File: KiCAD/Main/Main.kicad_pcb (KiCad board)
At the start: 4 copper layers, 61.8 x 150 mm, 98 parts, among them J1 Micro_SD_Card_Det2, J2 Screw_Terminal_01x09, J3 Screw_Terminal_01x09, J4 USB_C_Receptacle_USB2.0_16P, J7 Conn_02x05_Top_Bottom_Mountin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, J8 Conn_Coaxial, J9 Conn_Coaxial, Q1 AO3400A, Q2 AO3400A, Q3 AO3400A, Q4 2N7002, SW1 RESET, SW2 USER, U1 LM2596S-3.3, U11 BMP390L, U12 BMP390L, U13 BMP390L, U14 BMI270, U15 BMI270, U16 BMI270, U17 SHT4x, U2 TPS2121RUXR, U3 BMM350, U4 STM32H750VBTx, U5 MAX-M8Q, U7 ISM6HG256x, Y2 SiT8008xx-2x-xxE (25MHz)

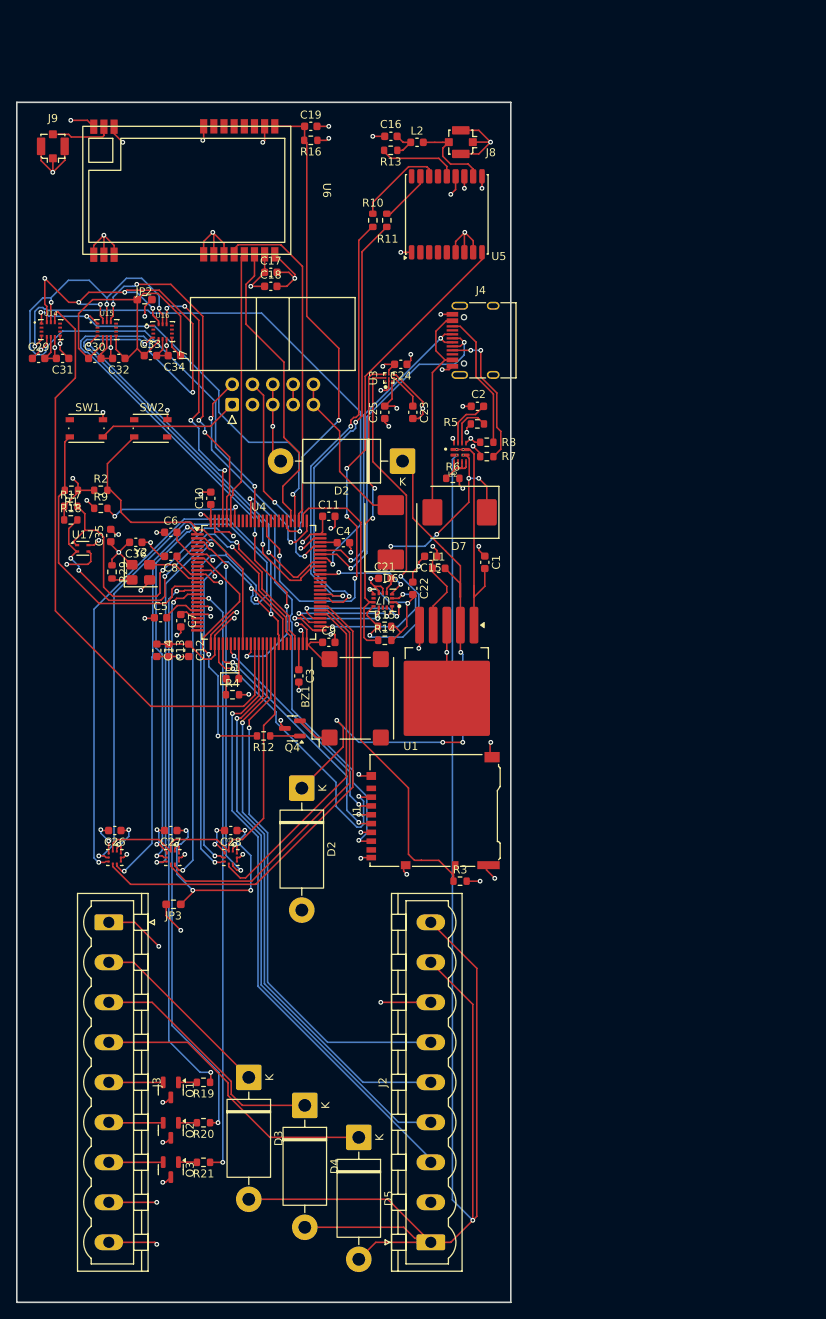
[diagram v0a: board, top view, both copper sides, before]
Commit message: Initial component placement
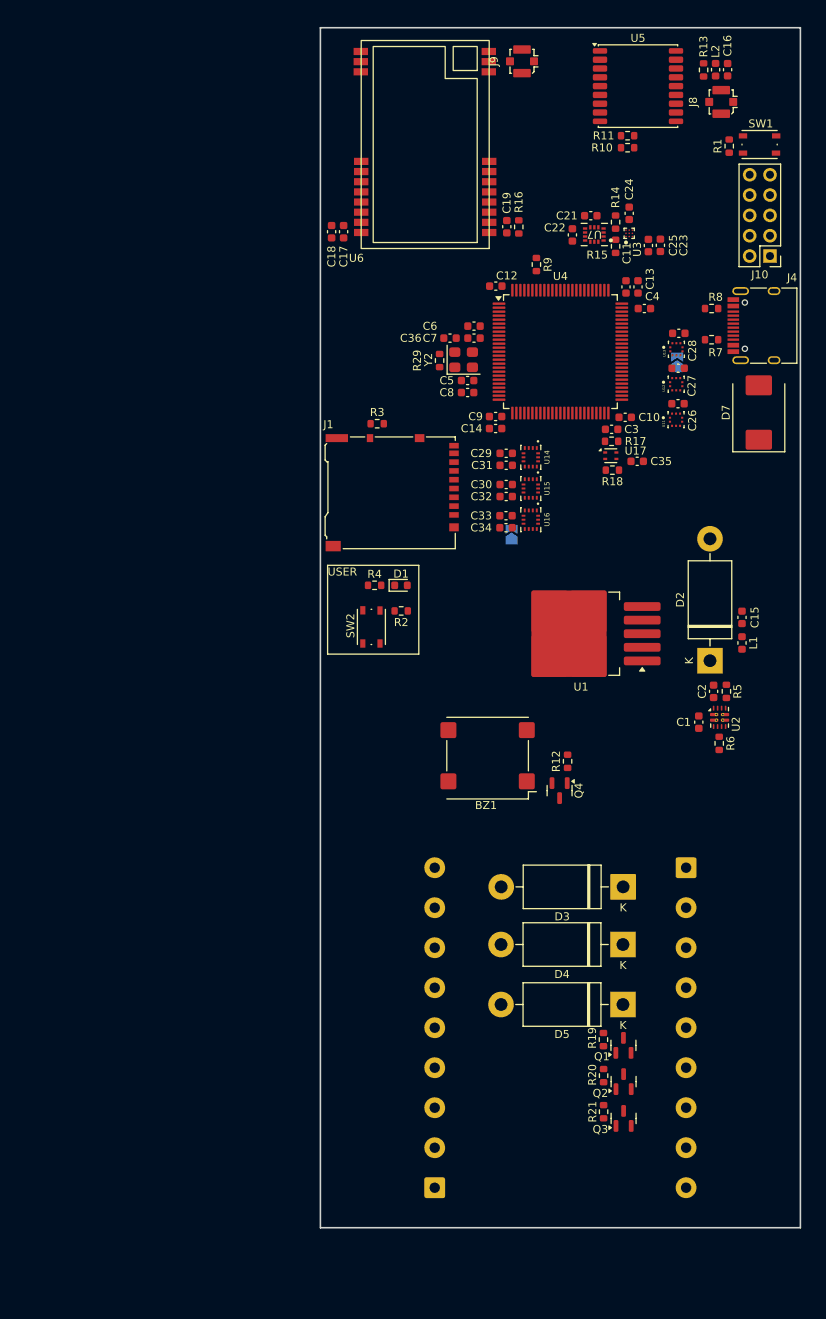
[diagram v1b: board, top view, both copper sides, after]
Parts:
- removed the D2 at (118.0, 84.8)
- removed the D2 at (105.4, 125.7)
- removed D6: MBRS340, Diode_SMD:D_SMC
- removed J7: Conn_02x05_Top_Bottom_MountingPin, Connector_IDC:IDC-Header_2x05_P2.54mm_Horizontal
- added D2: 1N5820, Diode_THT:D_DO-201AD_P15.24mm_Horizontal, F.Cu at (156.4, 109.8)
- added J10: Conn_02x05_Counter_Clockwise, Connector_PinHeader_2.54mm:PinHeader_2x05_P2.54mm_Vertical, F.Cu at (163.9, 59.2)
- J2, J3: footprint Connector_Phoenix_MSTB:PhoenixContact_MSTBVA_2,5_9-G_1x09_P5.00mm_Vertical -> TerminalBlock_Phoenix:TerminalBlock_Phoenix_MKDS-1,5-9_1x09_P5.00mm_Horizontal; moved to B.Cu
- JP2, JP3: footprint Resistor_SMD:R_0603_1608Metric_Pad0.98x0.95mm_HandSolder -> Jumper:SolderJumper-2_P1.3mm_Open_TrianglePad1.0x1.5mm; moved to B.Cu
- U11, U12, U13: footprint BMP390L:XDCR_BMP390L -> LRI:XDCR_BMP390L
- U14, U15, U16: footprint BMI270:XDCR_BMI270 -> LRI:XDCR_BMI270
- U2: footprint TPS2121RUXR:IC_TPS2121RUXR -> Package_DFN_QFN:Texas_VQFN-HR-12_2x2.5mm_P0.5mm_ThermalVias
- U3: footprint BMM350:BGA9C40P3X3_128X128X50 -> LRI:BGA9C40P3X3_128X128X50
- U6: footprint E22-900T22S:E22-900T22S -> LRI:E22-900T22S
- U7: footprint ISM6HG256XTR:U_LGA-14L_2p5X3p0X0p83_STM -> LRI:ISM6
- moved R1 92.8 mm to (158.8, 45.5), turned to 90 degrees
- moved JP3 92.5 mm to (152.3, 72.5), turned to 90 degrees
- moved SW1 91.3 mm to (162.6, 45.3)
- moved U11 89.0 mm to (152.2, 79.7), turned to 90 degrees
- moved C26 88.3 mm to (152.4, 77.7), turned to 0 degrees
- moved U12 86.4 mm to (152.2, 75.2), turned to 90 degrees
- moved C27 85.8 mm to (152.4, 73.2), turned to 0 degrees
- moved U13 84.5 mm to (152.2, 70.9), turned to 90 degrees
- moved C28 83.7 mm to (152.5, 68.9), turned to 0 degrees
- moved C13 74.2 mm to (147.4, 63.1), turned to 90 degrees
- moved J3 72.5 mm to (153.4, 135.7)
- moved R17 68.1 mm to (144.1, 82.4), turned to 180 degrees
- moved R18 68.0 mm to (144.2, 86.0), turned to 180 degrees
- moved U17 67.0 mm to (144.0, 84.2)
- moved C35 66.5 mm to (147.3, 84.9), turned to 0 degrees
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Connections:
- R12 pad 2: Net-(U4-PC13) -> /Microcontroller/BUZZER
- U4 pad 1: /Barometer/BMP390 INT1 -> unconnected-(U4-PE2-Pad1)
- U4 pad 15: /Microcontroller/Drogue Eject Main -> unconnected-(U4-PC0-Pad15)
- U4 pad 16: /Microcontroller/Drogue Eject Backup -> unconnected-(U4-PC1-Pad16)
- U4 pad 17: /Microcontroller/Main Eject -> /Microcontroller/Servo1_Encoder
- U4 pad 18: unconnected-(U4-PC3_C-Pad18) -> /Microcontroller/Servo2_Encoder
- U4 pad 2: /Barometer/BMP390 INT2 -> unconnected-(U4-PE3-Pad2)
- U4 pad 25: unconnected-(U4-PA3-Pad25) -> /Microcontroller/SD_Det
- U4 pad 3: /Barometer/BMP390 INT3 -> /Microcontroller/Drogue Eject Main
- U4 pad 30: unconnected-(U4-PA6-Pad30) -> /Microcontroller/SD_MISO
- U4 pad 33: /Microcontroller/USER_LED -> unconnected-(U4-PC5-Pad33)
- U4 pad 34: /Microcontroller/USER_BTN -> unconnected-(U4-PB0-Pad34)
- U4 pad 35: /Microcontroller/SIMU CS3 -> unconnected-(U4-PB1-Pad35)
- U4 pad 36: /Microcontroller/SIMU MOSI -> /Microcontroller/SIMU1 INT
- U4 pad 38: /Microcontroller/Servo1_DOut -> /Microcontroller/SIMU2 INT
- U4 pad 39: /Microcontroller/Servo2_DOut -> /Microcontroller/SIMU CS2
- U4 pad 4: unconnected-(U4-PE5-Pad4) -> /Microcontroller/Drogue Eject Backup
- U4 pad 40: /Microcontroller/Servo1_Encoder -> /Microcontroller/SIMU3 INT
- U4 pad 41: /Microcontroller/Servo2_Encoder -> /Microcontroller/SIMU CS3
- U4 pad 42: /Barometer/BMP390_SCK -> /Microcontroller/SIMU CLK
- U4 pad 43: /Barometer/BMP390_MISO -> /Microcontroller/SIMU MISO
- U4 pad 44: /Barometer/BMP390_MOSI -> /Microcontroller/SIMU MOSI
- U4 pad 5: unconnected-(U4-PE6-Pad5) -> /Microcontroller/Main Eject
- U4 pad 51: /IMUs/BNO_CS -> unconnected-(U4-PB12-Pad51)
- U4 pad 52: /IMUs/BNO_SCK -> /Barometer/BMP390_SCK
- U4 pad 53: /IMUs/BNO_MISO -> /Barometer/BMP390_MISO
- U4 pad 54: /IMUs/BNO_MOSI -> /Barometer/BMP390_MOSI
- U4 pad 55: /Barometer/BMP390_CS3 -> /Barometer/BMP390_CS1
- U4 pad 56: /Barometer/BMP390_CS2 -> /Barometer/BMP390 INT1
- U4 pad 57: /Barometer/BMP390_CS1 -> /Barometer/BMP390_CS2
- U4 pad 58: unconnected-(U4-PD11-Pad58) -> /Barometer/BMP390 INT2
- U4 pad 59: /GPS/GPS_SCL -> /Barometer/BMP390_CS3
- U4 pad 60: /GPS/GPS_SDA -> /Barometer/BMP390 INT3
- U4 pad 63: unconnected-(U4-PC6-Pad63) -> /Microcontroller/Servo1_DOut
- U4 pad 64: unconnected-(U4-PC7-Pad64) -> /Microcontroller/Servo2_DOut
- U4 pad 65: /IMUs/BNO_INT -> /Microcontroller/BUZZER
- U4 pad 66: unconnected-(U4-PC9-Pad66) -> /Microcontroller/USER_LED
- U4 pad 67: /Microcontroller/SIMU3 INT -> /Microcontroller/USER_BTN
- U4 pad 68: /Microcontroller/SIMU2 INT -> unconnected-(U4-PA9-Pad68)
- U4 pad 69: /Microcontroller/SIMU1 INT -> unconnected-(U4-PA10-Pad69)
- U4 pad 7: Net-(U4-PC13) -> unconnected-(U4-PC13-Pad7)
- U4 pad 77: /Microcontroller/SD_Det -> /IMUs/ISM_INT
- U4 pad 78: /Microcontroller/Radio TX -> /IMUs/ISM_SCK
- U4 pad 79: /Microcontroller/SIMU MISO -> /IMUs/ISM_MISO
- U4 pad 80: /Microcontroller/Radio AUX -> /IMUs/ISM_MOSI
- U4 pad 81: /Microcontroller/Radio RST -> /IMUs/ISM_CS
- U4 pad 86: /GPS/GPS_RESET -> unconnected-(U4-PD5-Pad86)
- U4 pad 89: /Microcontroller/SIMU CLK -> unconnected-(U4-PB3-Pad89)
- U4 pad 90: /Microcontroller/SD_MISO -> unconnected-(U4-PB4-Pad90)
- U4 pad 91: unconnected-(U4-PB5-Pad91) -> /GPS/GPS_RESET
- U4 pad 92: unconnected-(U4-PB6-Pad92) -> /GPS/GPS_SCL
- U4 pad 93: unconnected-(U4-PB7-Pad93) -> /GPS/GPS_SDA
- U4 pad 95: /Microcontroller/Radio RX -> /Microcontroller/Radio RST
- U4 pad 96: unconnected-(U4-PB9-Pad96) -> /Microcontroller/Radio AUX
- U4 pad 97: /Microcontroller/SIMU CS2 -> /Microcontroller/Radio RX
- U4 pad 98: unconnected-(U4-PE1-Pad98) -> /Microcontroller/Radio TX
- U7 pad 1: /IMUs/BNO_MISO -> /IMUs/ISM_MISO
- U7 pad 10: Net-(U3-SCK) -> unconnected-(U7-OCS_Aux-Pad10)
- U7 pad 11: Net-(U3-SDA) -> unconnected-(U7-SDO_Aux-Pad11)
- U7 pad 12: /IMUs/BNO_CS -> /IMUs/ISM_CS
- U7 pad 13: unconnected-(U7-SCL-Pad13) -> /IMUs/ISM_SCK
- U7 pad 14: unconnected-(U7-SDA-Pad14) -> /IMUs/ISM_MOSI
- U7 pad 2: /IMUs/BNO_MOSI -> Net-(U3-SDA)
- U7 pad 3: /IMUs/BNO_SCK -> Net-(U3-SCK)
- U7 pad 4: /IMUs/BNO_INT -> /IMUs/ISM_INT
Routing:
- net GND: track 238.3 -> 0.00 mm, vias 80 -> 0
- net Net-(D3-A): track 229.0 -> 0.00 mm, vias 1 -> 0
- net /Barometer/BMP390_MISO: track 172.7 -> 0.00 mm, vias 5 -> 0
- net /Barometer/BMP390_MOSI: track 167.2 -> 0.00 mm, vias 4 -> 0
- net +3V3: track 157.9 -> 0.00 mm, vias 28 -> 0
- net /Microcontroller/SIMU MOSI: track 121.9 -> 0.00 mm, vias 9 -> 0
- net /Microcontroller/SIMU CLK: track 80.7 -> 0.00 mm, vias 4 -> 0
- net /Microcontroller/SIMU CS1: track 77.7 -> 0.00 mm
- net /Microcontroller/Servo1_DOut: track 77.1 -> 0.00 mm, vias 1 -> 0
- net /Microcontroller/SIMU1 INT: track 74.7 -> 0.00 mm, vias 2 -> 0
- net /Microcontroller/Main Eject: track 74.2 -> 0.00 mm, vias 2 -> 0
- net /Microcontroller/Servo2_DOut: track 73.8 -> 0.00 mm, vias 1 -> 0
- net /Microcontroller/Drogue Eject Backup: track 72.2 -> 0.00 mm, vias 2 -> 0
- net /Microcontroller/Servo1_Encoder: track 71.0 -> 0.00 mm, vias 1 -> 0
- net Net-(D2-K): track 70.5 -> 0.00 mm, vias 4 -> 0
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- removed copper zone on In2.Cu, net +3V3
- removed copper zone on In1.Cu, net GND
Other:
- board size 61.8 x 150 mm -> 60 x 150 mm
- board text added: "USER"

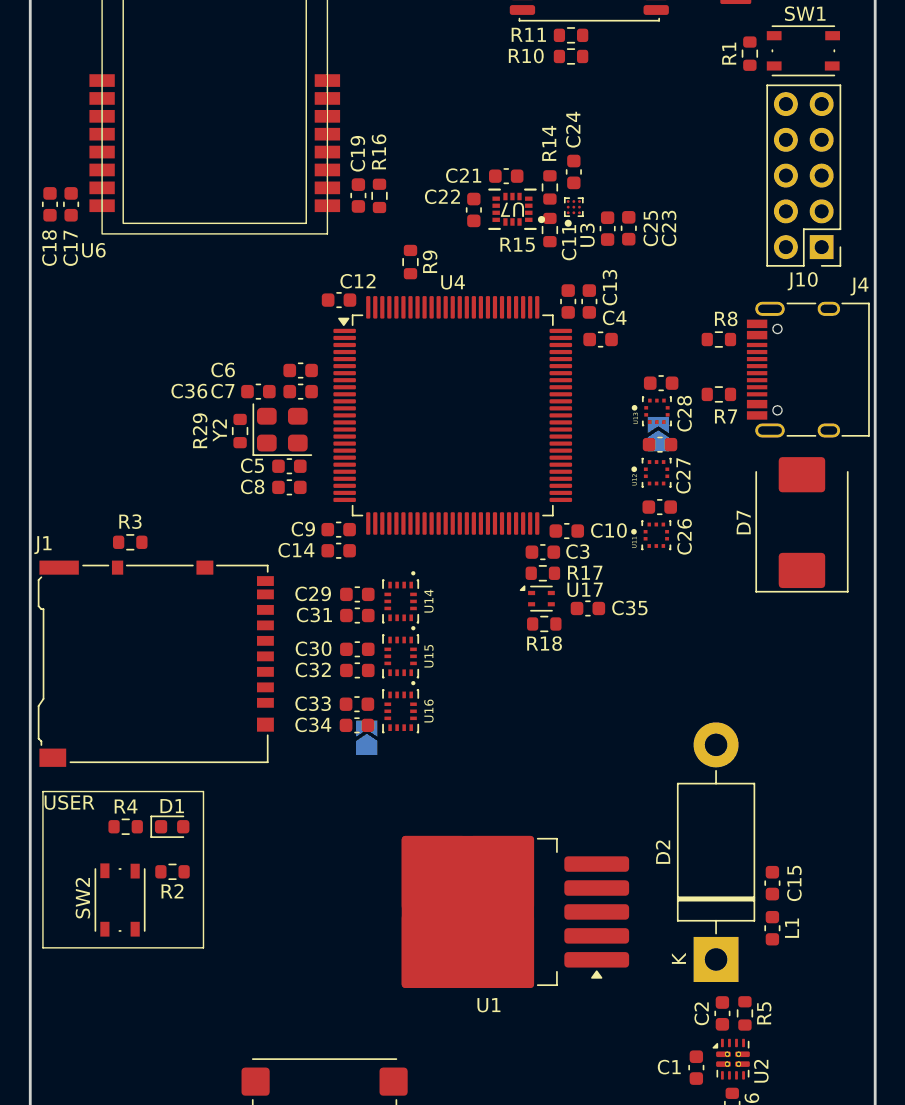
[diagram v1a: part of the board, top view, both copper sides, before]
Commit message: Fixed routing for LIS2MDL
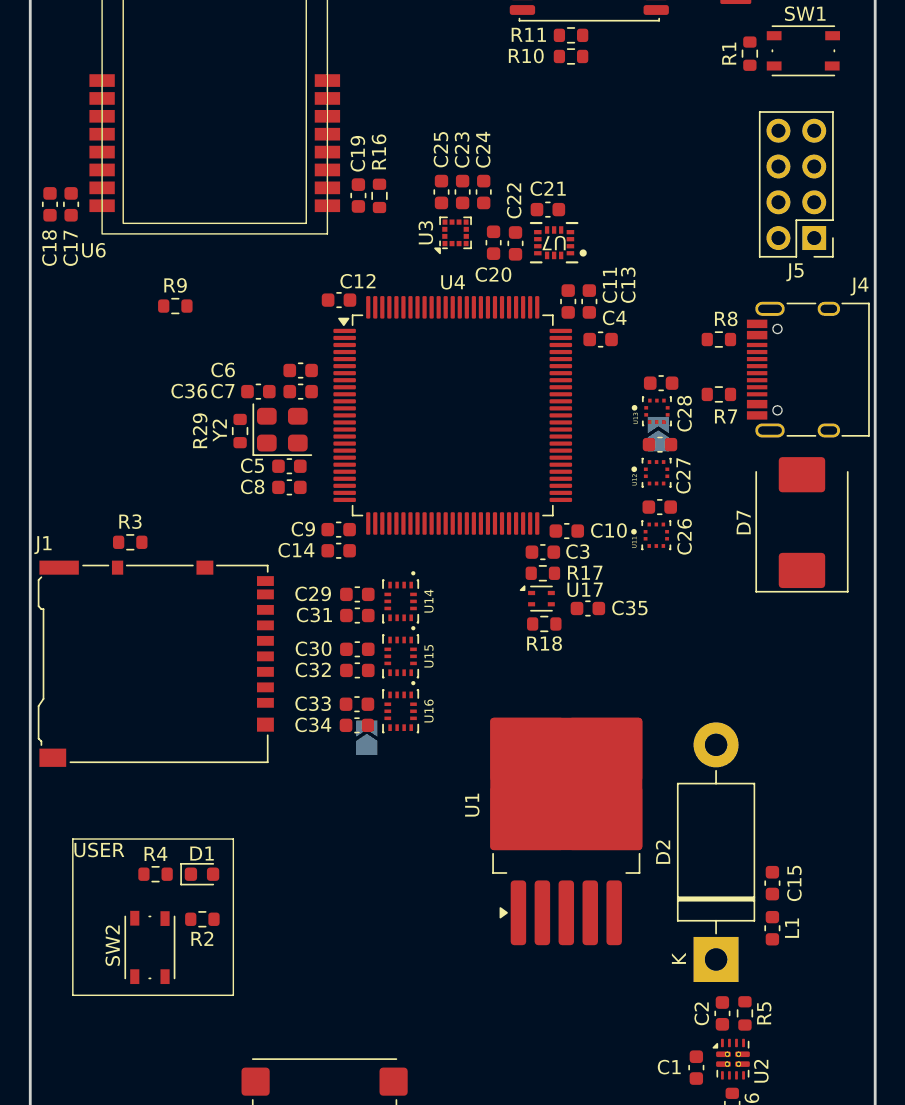
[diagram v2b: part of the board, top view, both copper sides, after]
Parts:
- removed J10: Conn_02x05_Counter_Clockwise, Connector_PinHeader_2.54mm:PinHeader_2x05_P2.54mm_Vertical
- removed R14, R15: 10k, Resistor_SMD:R_0603_1608Metric
- added C20: 220n, Capacitor_SMD:C_0603_1608Metric, F.Cu at (140.6, 58.9)
- added J5: Conn_02x04_Counter_Clockwise, Connector_PinHeader_2.54mm:PinHeader_2x04_P2.54mm_Vertical, F.Cu at (163.4, 58.6)
- C23: value 2.2u -> 100n
- C24: value 100n -> 10u
- U3: value BMM350 -> LIS2MDL; footprint LRI:BGA9C40P3X3_128X128X50 -> Package_LGA:LGA-12_2x2mm_P0.5mm
- moved R9 17.0 mm to (118.0, 63.4), turned to 0 degrees
- moved C25 12.1 mm to (136.9, 55.3)
- moved C23 12.1 mm to (138.4, 55.3), turned to 90 degrees
- moved U1 9.37 mm to (145.8, 98.8), turned to 90 degrees
- moved U3 8.60 mm to (137.9, 58.2)
- moved C24 6.56 mm to (139.9, 55.3), turned to 90 degrees
- moved R4 3.98 mm to (116.6, 103.7)
- moved D1 3.98 mm to (119.9, 103.7)
- moved R2 3.98 mm to (119.9, 106.9)
- moved SW2 3.98 mm to (116.2, 108.9)
- moved C21 3.79 mm to (144.5, 56.6)
- moved C22 3.79 mm to (142.2, 59.0)
- moved U7 3.79 mm to (144.9, 58.9)
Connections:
- C23 pad 1: Net-(U3-CRST) -> +3V3
- C24 pad 1: GND -> +3V3
- C24 pad 2: +3V3 -> GND
- C25 pad 1: GND -> +3V3
- C25 pad 2: +3V3 -> GND
- U4 pad 1: unconnected-(U4-PE2-Pad1) -> /Microcontroller/Radio RST
- U4 pad 2: unconnected-(U4-PE3-Pad2) -> /Microcontroller/Radio AUX
- U4 pad 90: unconnected-(U4-PB4-Pad90) -> /IMUs/INT_LIS
- U4 pad 92: /GPS/GPS_SCL -> /IMUs/SCL_LIS
- U4 pad 93: /GPS/GPS_SDA -> /IMUs/SDA_LIS
- U4 pad 95: /Microcontroller/Radio RST -> /GPS/GPS_SCL
- U4 pad 96: /Microcontroller/Radio AUX -> /GPS/GPS_SDA
- U7 pad 2: Net-(U3-SDA) -> unconnected-(U7-SDx-Pad2)
- U7 pad 3: Net-(U3-SCK) -> unconnected-(U7-SCx-Pad3)

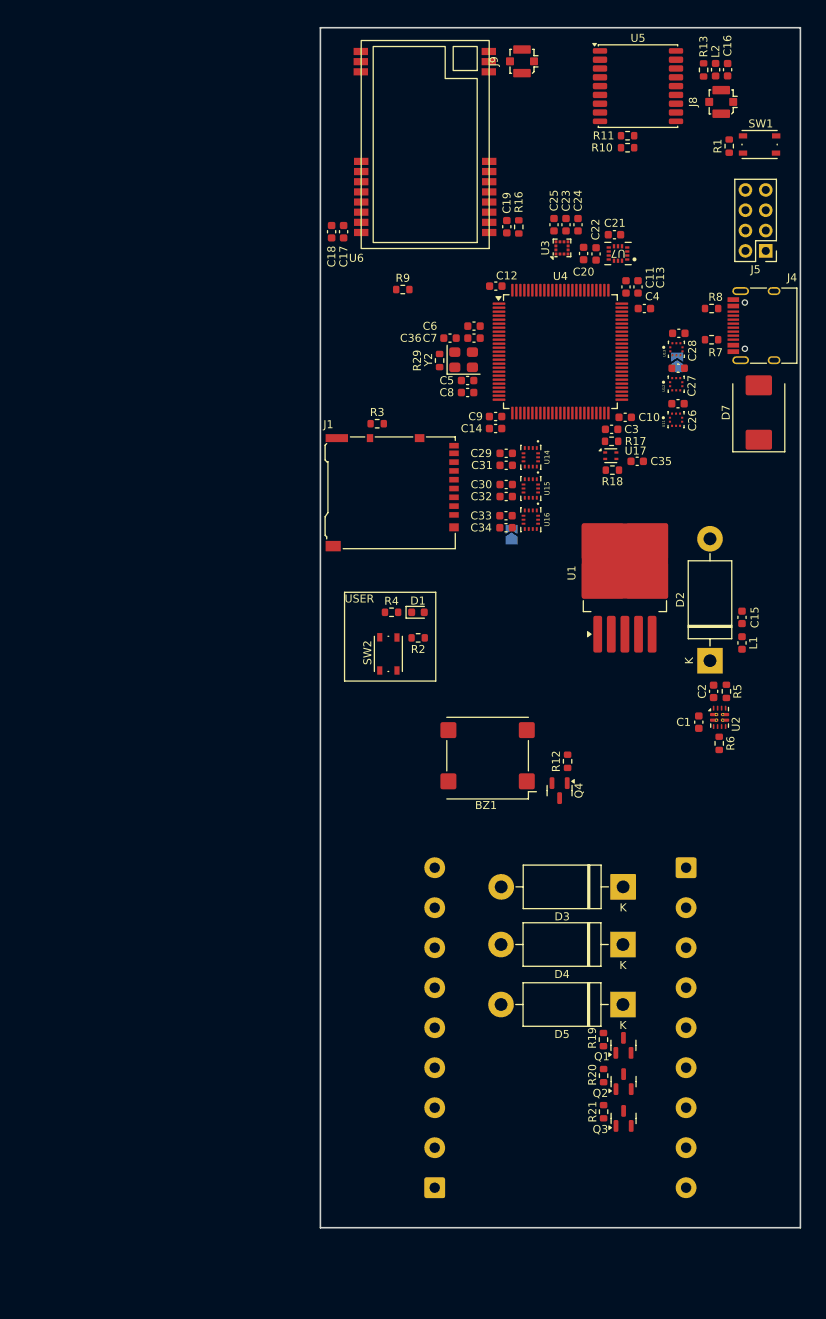
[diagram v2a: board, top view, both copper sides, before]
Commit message: DRC and ground fills
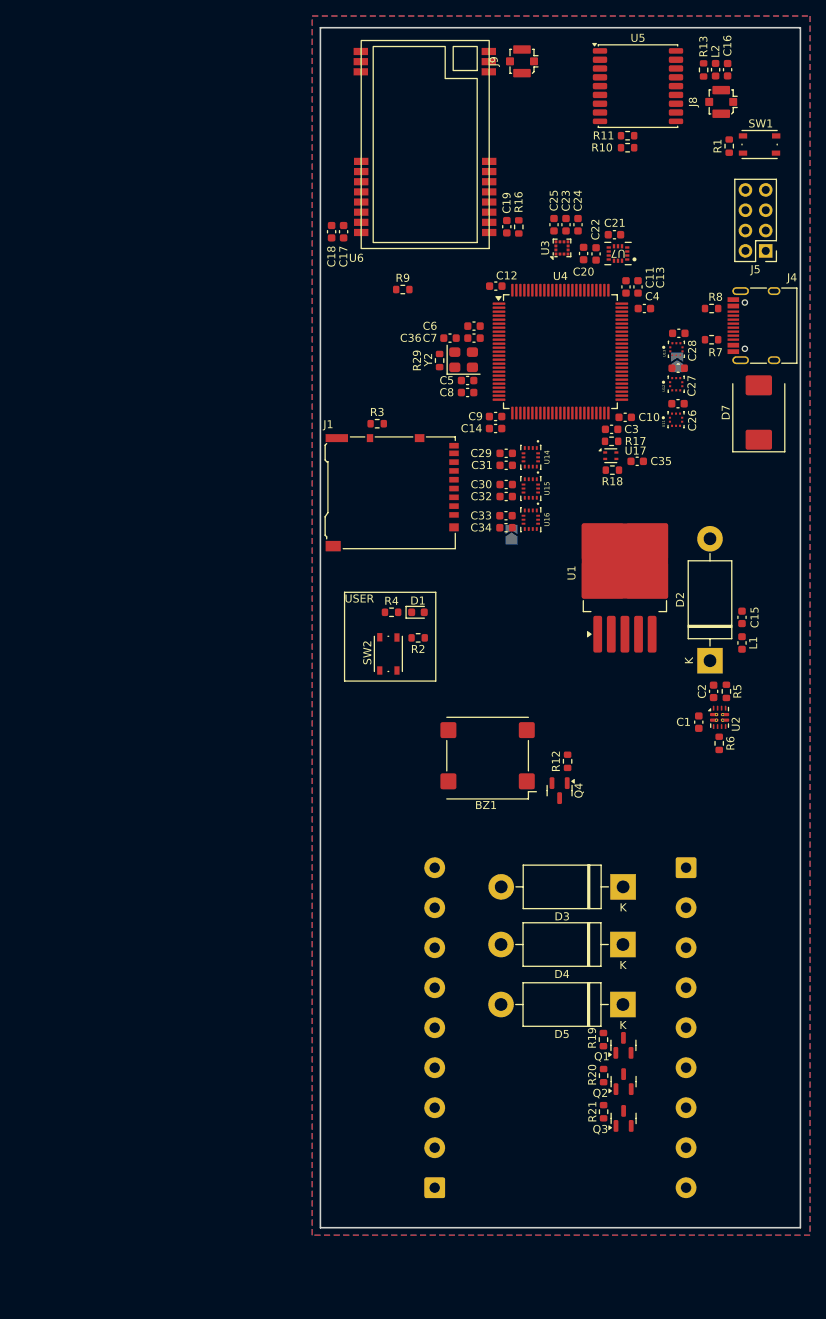
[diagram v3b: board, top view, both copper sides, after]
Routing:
- added copper zone on In2.Cu, net +3V3
- added copper zone on B.Cu, net GND
- added copper zone on F.Cu, net GND
- added copper zone on In1.Cu, net GND
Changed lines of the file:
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@@
+		)
+	)
+	(zone
+		(net 3)
+		(net_name "GND")
+		(layers "F.Cu" "B.Cu" "In1.Cu")
+		(hatch edge 0.5)
+		(connect_pads
+			(clearance 0.5)
+		)
+		(min_thickness 0.25)
+		(filled_areas_thickness no)
+		(fill yes
+			(thermal_gap 0.5)
+			(thermal_bridge_width 0.5)
+		)
+		(polygon
+			(pts
+				(xy 106.68 29.21) (xy 168.91 29.21) (xy 168.91 181.61) (xy 106.68 181.61)
+			)
+		)
+	)
+	(zone
+		(net 2)
+		(net_name "+3V3")
+		(layer "In2.Cu")
+		(hatch edge 0.5)
+		(priority 1)
+		(connect_pads
+			(clearance 0.5)
+		)
+		(min_thickness 0.25)
+		(filled_areas_thickness no)
+		(fill yes
+			(thermal_gap 0.5)
+			(thermal_bridge_width 0.5)
+		)
+		(polygon
+			(pts
+				(xy 106.68 29.21) (xy 168.91 29.21) (xy 168.91 181.61) (xy 106.68 181.61)
+			)
 		)
 	)
